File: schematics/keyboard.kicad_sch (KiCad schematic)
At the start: 35 parts, among them J2 Mini-DIN-6, Q1 2N7000, Q2 2N7000, Q3 2N7000, Q4 2N7000, Q5 2N7000, U18 74HC14, U19 74HC04, U21 ATF22V10C-7, U22 74HC280, U23 74HC165, U24 74HC595, U25 74HC165, U26 74HC595, U37 74HC245

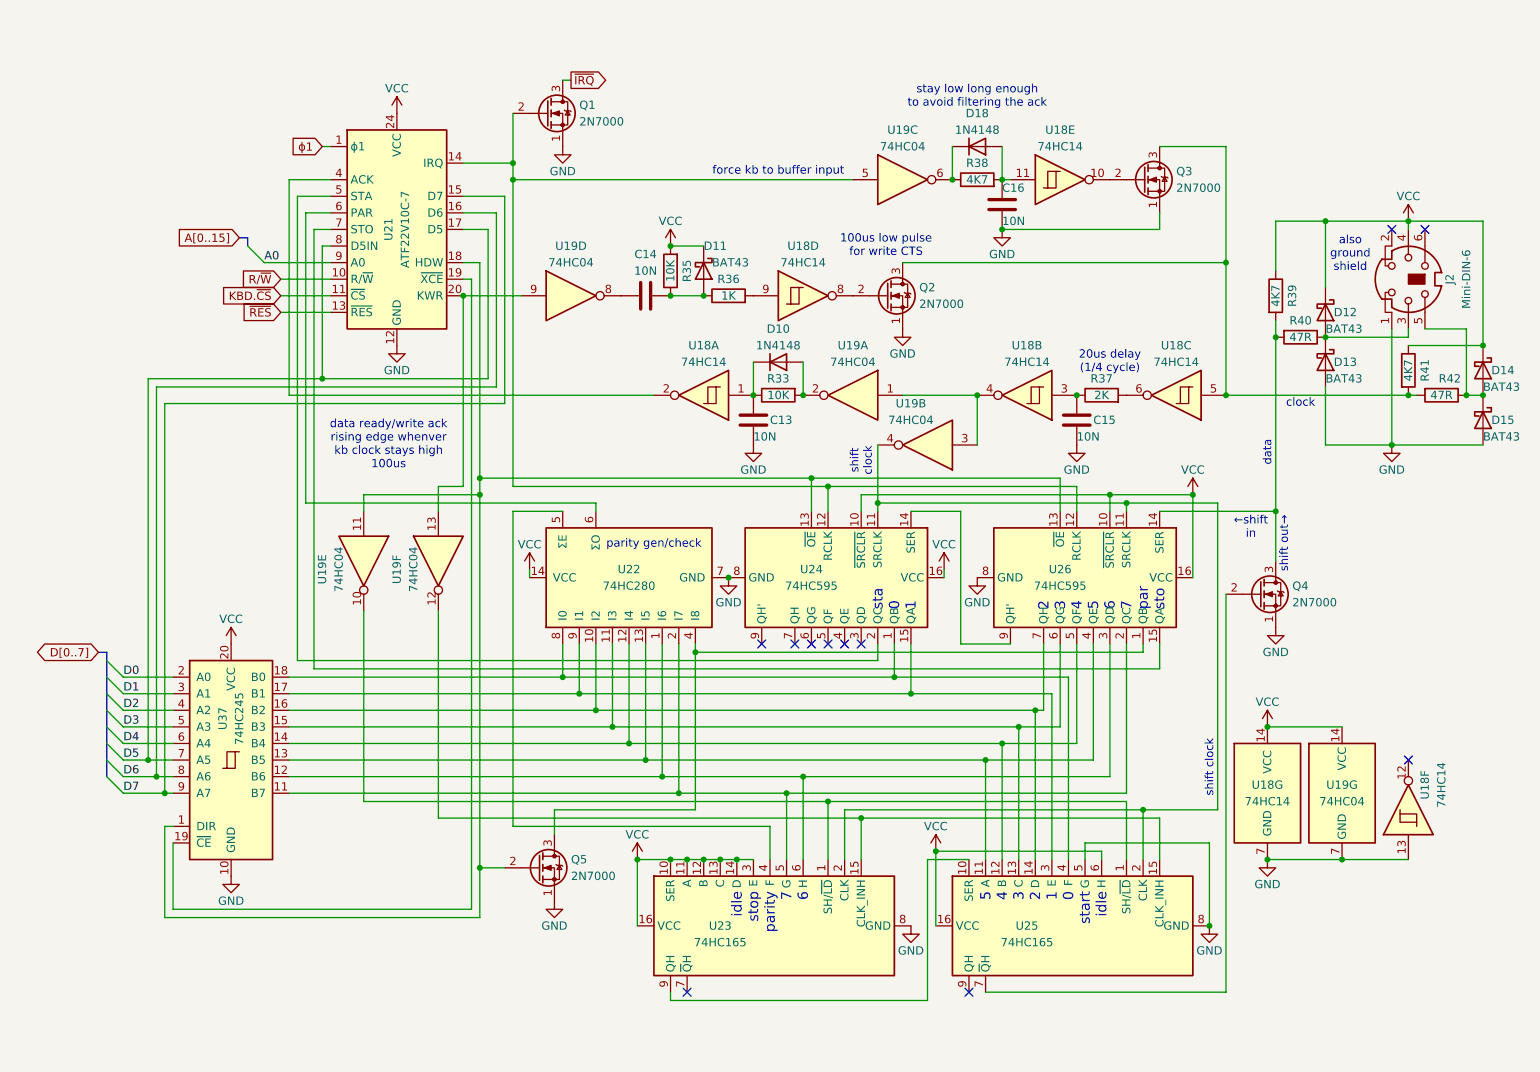
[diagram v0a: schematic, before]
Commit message: keyboard LEDs work
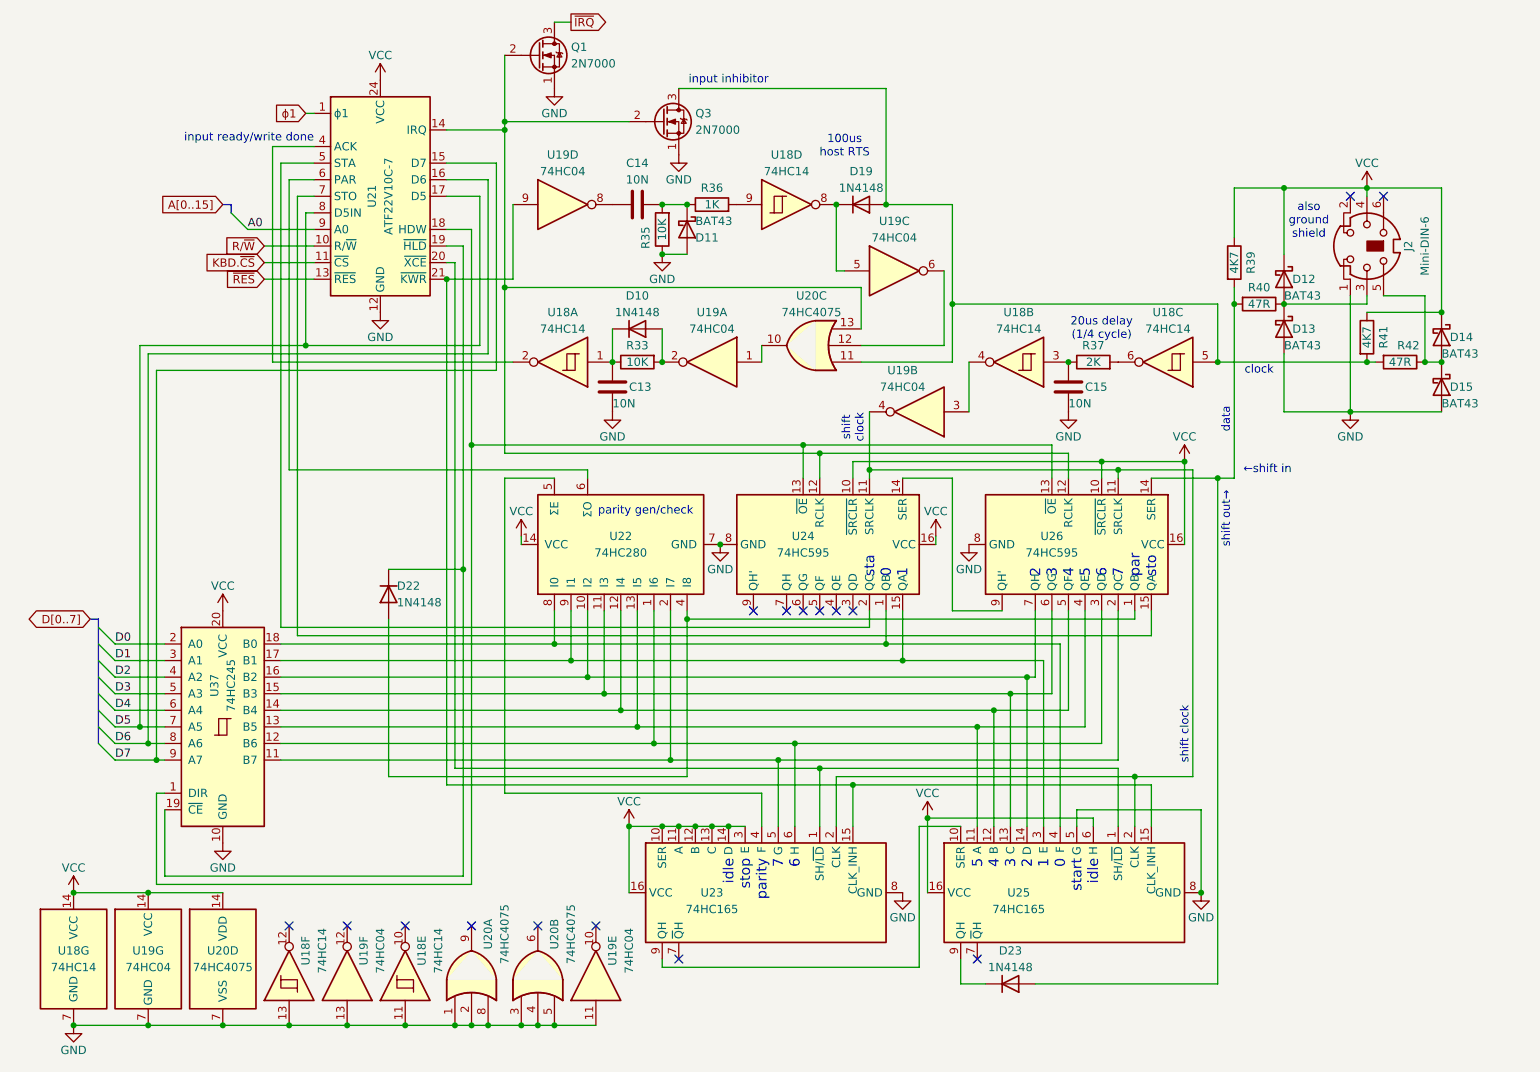
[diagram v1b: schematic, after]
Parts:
- removed C16: 10N, symbol Device:C
- removed D18: 1N4148, Diode_THT:D_DO-35_SOD27_P7.62mm_Horizontal, symbol Diode:1N4148
- removed Q2, Q4, Q5: 2N7000, Package_TO_SOT_THT:TO-92_Inline, symbol Transistor_FET:2N7000
- removed R38: 4K7, symbol Device:R
- added D19, D22, D23: 1N4148, Diode_THT:D_DO-35_SOD27_P7.62mm_Horizontal, symbol Diode:1N4148
- added U20: 74HC4075, symbol 4xxx:4075
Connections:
- net GND: now also D11.2 (A), R35.1, U18.11, U19.11, U19.13, U20.1, U20.2, U20.3, U20.4, U20.5, U20.7 (VSS), U20.8
- net VCC: now also U20.14 (VDD); no longer D11.1 (K), R35.2
- net at U18.10: no longer Q3.2 (G)
- net at U18.4, U19.3: no longer U19.1
- net at U21.18 (HDW), U24.13 (~{OE}), U26.13 (~{OE})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: no longer U19.11
- net at U22.4 (I8), U26.1 (QB): now also D22.2 (A)
- net at Q1.2 (G), U21.14 (IRQ), U24.12 (RCLK)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: now also Q3.2 (G), U20.13; no longer U19.5
- net at U23.1 (SH/~{LD}), U25.1 (SH/~{LD}): now also U21.20 (~{XCE}); no longer U19.10
- net at U18.8: now also U19.5, D19.1 (K)
- net at Q3.3 (D), R41.2, R42.2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: now also D19.2 (A), U20.11
- net at U19.6: now also U20.12
- net at C14.2, R36.1: now also D11.1 (K), R35.2; no longer D11.2 (A), R35.1
- net at U21.19 (~{HLD}), U37.19 (~{CE}): now also D22.1 (K)
- net at U21.21 (~{KWR}): now also U19.9, U23.15 (CLK_INH), U25.15 (CLK_INH)
- net at R39.2, R40.2, U26.14 (SER): now also D23.2 (A)
- net at U25.9 (QH): now also D23.1 (K)
- new net: U19.1, U20.10
- now unconnected: U19.12
- no-connect marks 11 -> 16
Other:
- note added: "100us host RTS"
- note added: "input inhibitor"
- note added: "input ready/write done"
- note removed: "100us low pulse for write CTS"
- note removed: "data ready/write ack rising edge whenver kb clock stays high 100us"
- note removed: "force kb to buffer input"
- note removed: "stay low long enough to avoid filtering the ack"
- moved on the sheet: C13, C14, C15, D10, D11, D12, D13, D14, D15, J2, Q1, Q3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
